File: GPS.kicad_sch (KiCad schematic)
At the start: 7 parts, among them Q3 BC817

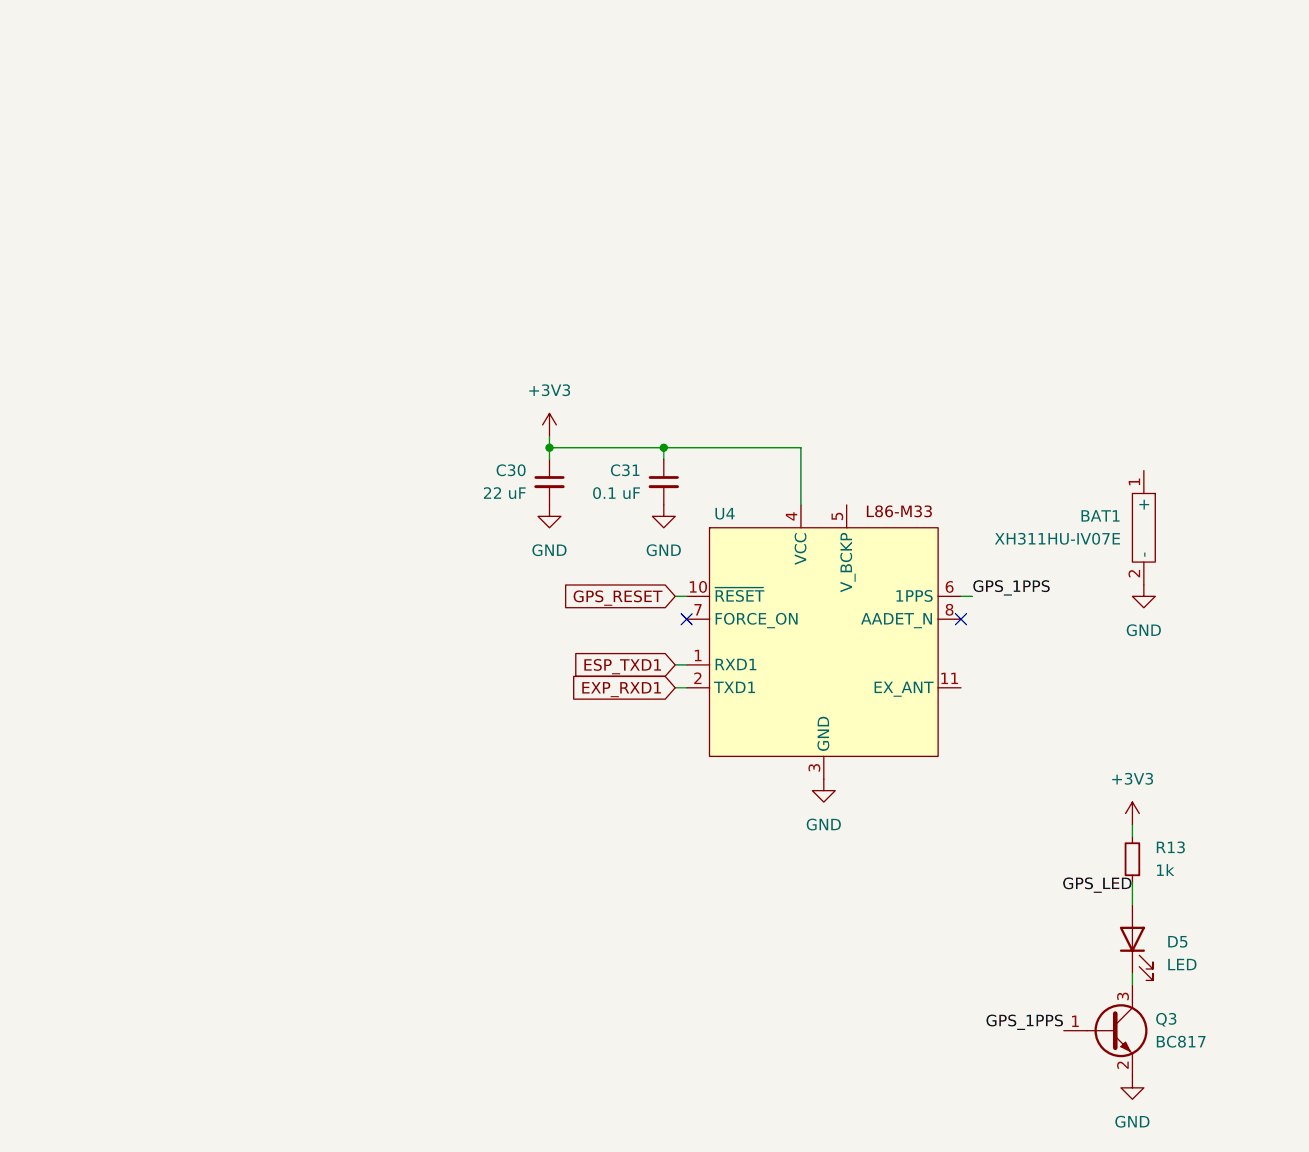
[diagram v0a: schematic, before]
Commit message: Wired barometers and GPS up, added misc LEDs, tidy-up
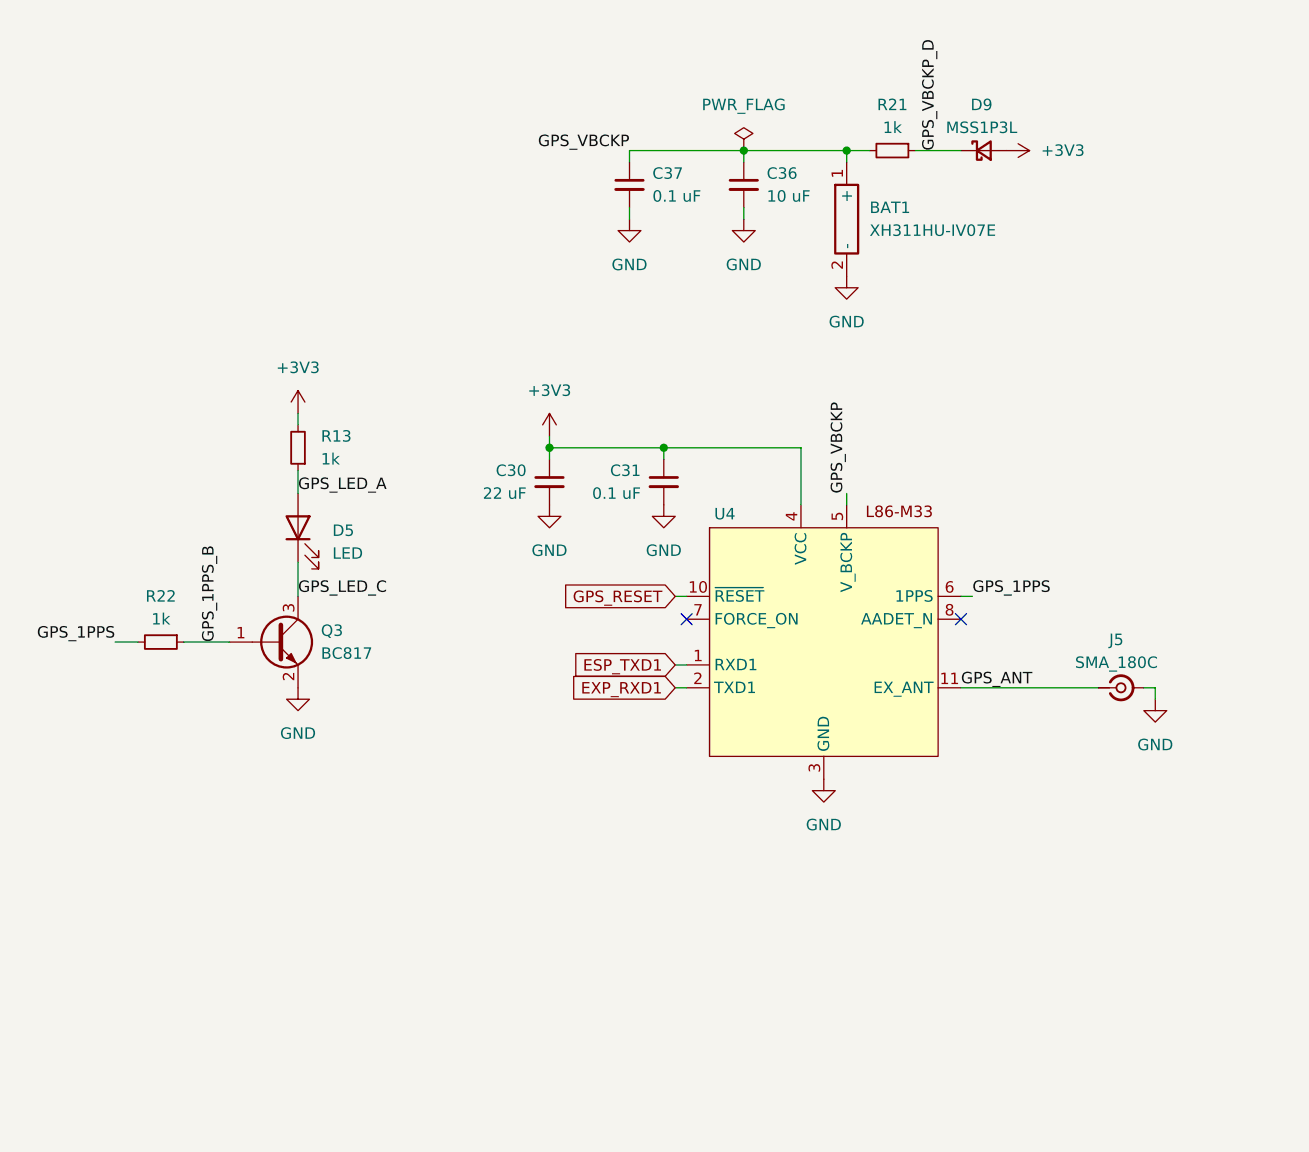
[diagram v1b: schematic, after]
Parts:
- added C36: 10 uF, symbol Device:C_Small
- added C37: 0.1 uF, Capacitor_SMD:C_0805_2012Metric, symbol Device:C_Small
- added D9: MSS1P3L, Diode_SMD:D_MicroSMP_AK, symbol Device:D_Schottky_Small
- added J5: SMA_180C, Valkyrie_footprints:SMA_180C, symbol Connector:Conn_Coaxial_Small
- added R21, R22: 1k, symbol Device:R_Small
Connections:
- net +3V3: now also D9.2 (A)
- net GND: now also C36.2, C37.2, J5.2 (Ext)
- net GPS_1PPS: now also R22.2; no longer Q3.1 (B)
- net GPS_LED_C: now reaches D5.1 (K), Q3.3 (C)
- net GPS_VBCKP: now reaches BAT1.1 (+)
- net GPS_VBCKP: now also U4.5 (V_BCKP), C36.1, C37.1, R21.2
- net GPS_ANT: now reaches U4.11 (EX_ANT)
- net GPS_ANT: now also J5.1 (In)
- net GPS_LED renamed GPS_LED_A
- new net GPS_1PPS_B: Q3.1 (B), R22.1
- new net GPS_VBCKP_D: D9.1 (K), R21.1
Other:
- moved on the sheet: BAT1, D5, Q3, R13

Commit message: preliminary schematic wired, all footprints assigned, all laid out in PCB editor.
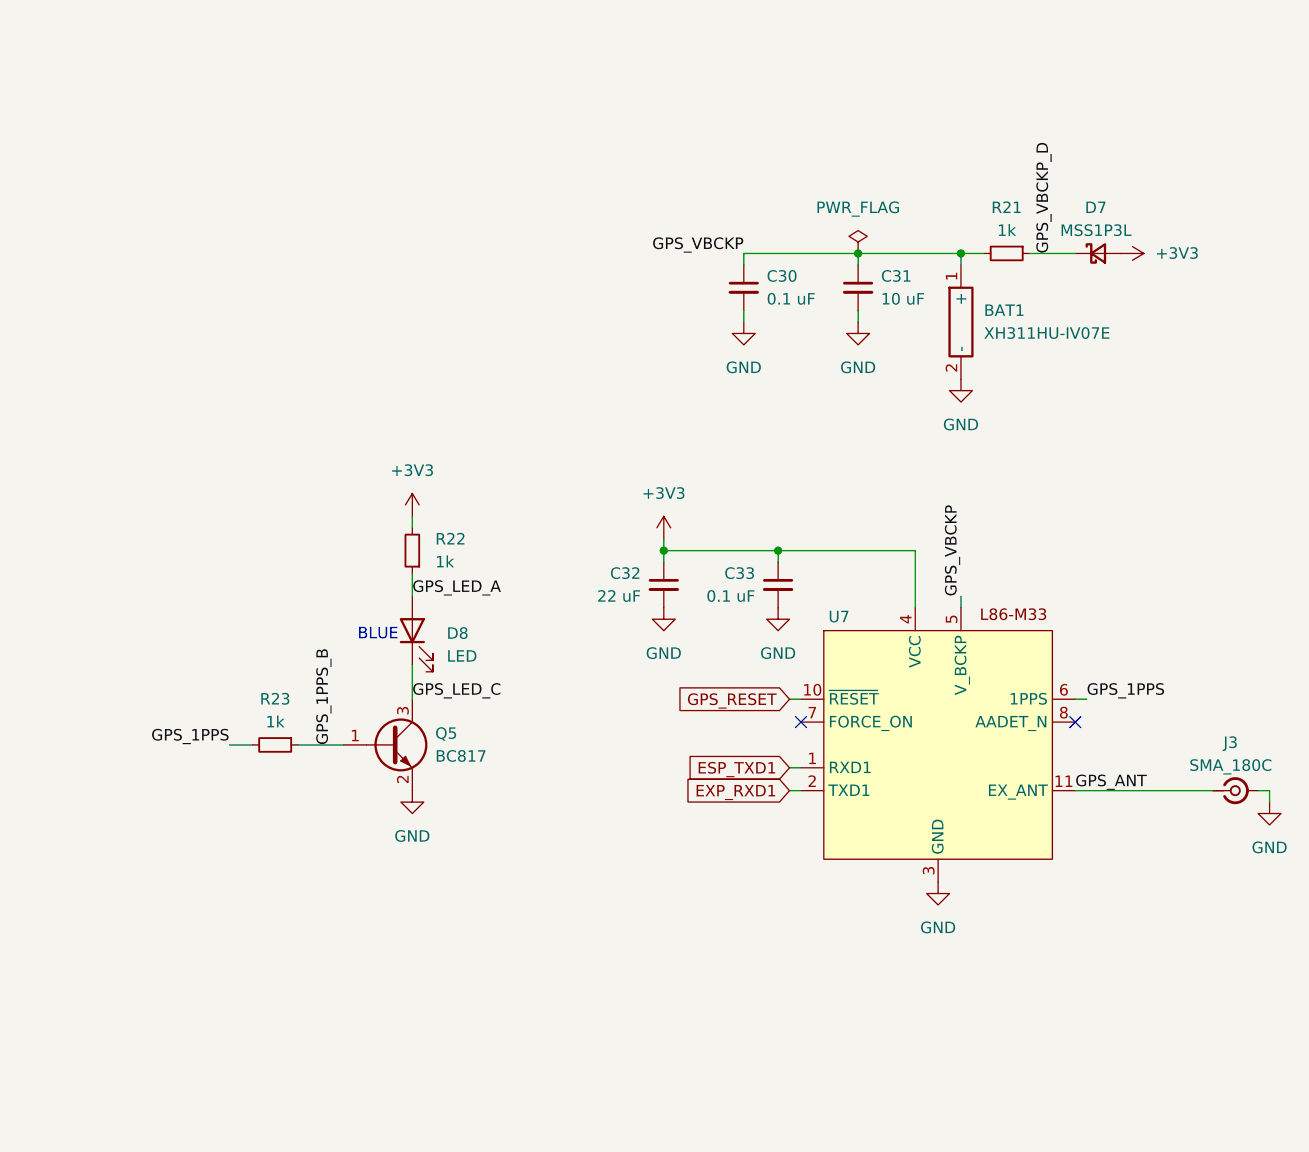
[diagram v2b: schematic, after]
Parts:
- C31: renamed from C36; footprint (none) -> Capacitor_SMD:C_0603_1608Metric
- C32: renamed from C30; footprint (none) -> Capacitor_SMD:C_0603_1608Metric
- R21: footprint (none) -> Resistor_SMD:R_0603_1608Metric
- R22: renamed from R13; footprint (none) -> Resistor_SMD:R_0603_1608Metric
- R23: renamed from R22; footprint (none) -> Resistor_SMD:R_0603_1608Metric
- renumbered C37 to C30, C31 to C33, D9 to D7, D5 to D8, J5 to J3, Q3 to Q5, U4 to U7
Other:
- note added: "BLUE"
- moved on the sheet: BAT1, C30, C31, C32, C33, D7, D8, J3, Q5, R21, R22, R23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

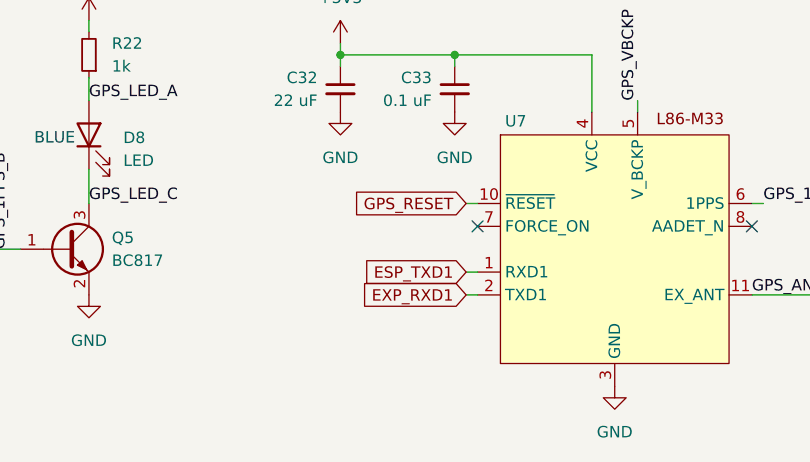
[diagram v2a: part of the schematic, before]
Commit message: reassigned some footprints, preliminary PCB layout
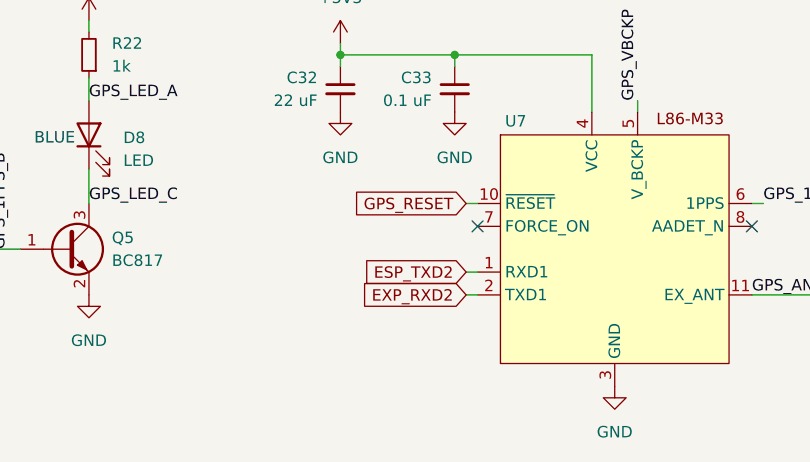
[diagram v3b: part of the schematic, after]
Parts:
- C30, C33: footprint Capacitor_SMD:C_0805_2012Metric -> Capacitor_SMD:C_0603_1608Metric
- D8: footprint LED_SMD:LED_0805_2012Metric -> LED_SMD:LED_0603_1608Metric
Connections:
- net ESP_TXD1 renamed ESP_TXD2
- net EXP_RXD1 renamed EXP_RXD2
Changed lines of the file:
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@@
 		)
 	)
-	(global_label "ESP_TXD1"
+	(global_label "ESP_TXD2"
 		(shape input)
 		(at 133.35 101.6 180)
@@
 		)
 	)
-	(global_label "EXP_RXD1"
+	(global_label "EXP_RXD2"
 		(shape input)
 		(at 133.35 104.14 180)
@@
 			)
 		)
-		(property "Footprint" "Capacitor_SMD:C_0805_2012Metric"
+		(property "Footprint" "Capacitor_SMD:C_0603_1608Metric"
 			(at 128.27 48.26 0)
 			(effects
@@
 			)
 		)
-		(property "Footprint" "Capacitor_SMD:C_0805_2012Metric"
+		(property "Footprint" "Capacitor_SMD:C_0603_1608Metric"
 			(at 132.08 81.28 0)
 			(effects
@@
 			)
 		)
-		(property "Footprint" "LED_SMD:LED_0805_2012Metric"
+		(property "Footprint" "LED_SMD:LED_0603_1608Metric"
 			(at 91.44 86.36 0)
 			(effects

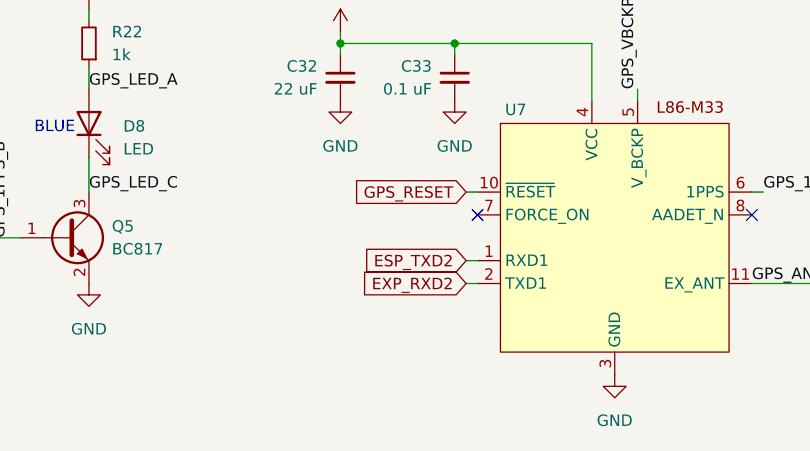
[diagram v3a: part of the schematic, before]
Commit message: added missing output diodes, added 3d models, misc. re-laying
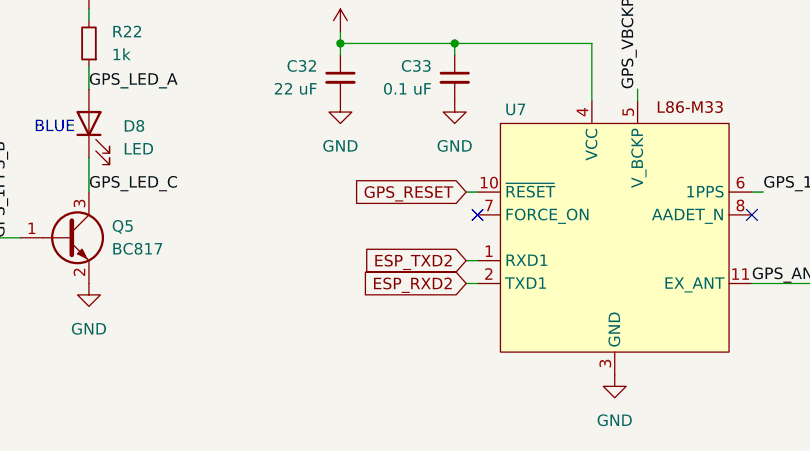
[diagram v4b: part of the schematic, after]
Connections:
- net EXP_RXD2 renamed ESP_RXD2
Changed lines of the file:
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@@
 		)
 	)
-	(global_label "EXP_RXD2"
+	(global_label "ESP_RXD2"
 		(shape input)
 		(at 133.35 104.14 180)

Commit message: did some clean-up, did some to-do tasks.
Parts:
- J3: footprint Valkyrie_footprints:SMA_180C -> Connector_Coaxial:SMA_Amphenol_132134-16_Vertical
- renumbered D7 to D8, D8 to D9
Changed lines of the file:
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@@
 		(dnp no)
 		(fields_autoplaced yes)
-		(property "Reference" "#PWR077"
+		(property "Reference" "#PWR080"
 			(at 119.38 80.01 0)
 			(effects
@@
 			(project "valkyriev3"
 				(path "/d24fd15c-a242-4d26-9876-7755ca0d378c/00fc6d2a-79f7-4b02-8c94-ea393adce81b"
-					(reference "#PWR077")
+					(reference "#PWR080")
 					(unit 1)
 				)
@@
 		(dnp no)
 		(fields_autoplaced yes)
-		(property "Reference" "#PWR073"
+		(property "Reference" "#PWR076"
 			(at 128.27 58.42 0)
 			(effects
@@
 			(project "valkyriev3"
 				(path "/d24fd15c-a242-4d26-9876-7755ca0d378c/00fc6d2a-79f7-4b02-8c94-ea393adce81b"
-					(reference "#PWR073")
+					(reference "#PWR076")
 					(unit 1)
 				)
@@
 		(dnp no)
 		(fields_autoplaced yes)
-		(property "Reference" "#PWR081"
+		(property "Reference" "#PWR084"
 			(at 186.69 111.76 0)
 			(effects
@@
 			(project "valkyriev3"
 				(path "/d24fd15c-a242-4d26-9876-7755ca0d378c/00fc6d2a-79f7-4b02-8c94-ea393adce81b"
-					(reference "#PWR081")
+					(reference "#PWR084")
 					(unit 1)
 				)
@@
 			)
 		)
-		(property "Footprint" "Valkyrie_footprints:SMA_180C"
+		(property "Footprint" "Connector_Coaxial:SMA_Amphenol_132134-16_Vertical"
 			(at 182.88 104.14 0)
 			(effects
@@
 		(dnp no)
 		(fields_autoplaced yes)
-		(property "Reference" "D8"
+		(property "Reference" "D9"
 			(at 95.25 86.6774 90)
 			(effects
@@
 			(project "valkyriev3"
 				(path "/d24fd15c-a242-4d26-9876-7755ca0d378c/00fc6d2a-79f7-4b02-8c94-ea393adce81b"
-					(reference "D8")
+					(reference "D9")
 					(unit 1)
 				)
@@
 		(dnp no)
 		(fields_autoplaced yes)
-		(property "Reference" "#PWR072"
+		(property "Reference" "#PWR075"
 			(at 166.37 44.45 0)
 			(effects
@@
 			(project "valkyriev3"
 				(path "/d24fd15c-a242-4d26-9876-7755ca0d378c/00fc6d2a-79f7-4b02-8c94-ea393adce81b"
-					(reference "#PWR072")
+					(reference "#PWR075")
 					(unit 1)
 				)
@@
 		(dnp no)
 		(fields_autoplaced yes)
-		(property "Reference" "#PWR079"
+		(property "Reference" "#PWR082"
 			(at 132.08 90.17 0)
 			(effects
@@
 			(project "valkyriev3"
 				(path "/d24fd15c-a242-4d26-9876-7755ca0d378c/00fc6d2a-79f7-4b02-8c94-ea393adce81b"
-					(reference "#PWR079")
+					(reference "#PWR082")
 					(unit 1)
 				)
@@
 		(dnp no)
 		(fields_autoplaced yes)
-		(property "Reference" "#PWR074"
+		(property "Reference" "#PWR077"
 			(at 140.97 58.42 0)
 			(effects
@@
 			(project "valkyriev3"
 				(path "/d24fd15c-a242-4d26-9876-7755ca0d378c/00fc6d2a-79f7-4b02-8c94-ea393adce81b"
-					(reference "#PWR074")
+					(reference "#PWR077")
 					(unit 1)
 				)
@@
 		(dnp no)
 		(fields_autoplaced yes)
-		(property "Reference" "#PWR082"
+		(property "Reference" "#PWR085"
 			(at 149.86 120.65 0)
 			(effects
@@
 			(project ""
 				(path "/d24fd15c-a242-4d26-9876-7755ca0d378c/00fc6d2a-79f7-4b02-8c94-ea393adce81b"
-					(reference "#PWR082")
+					(reference "#PWR085")
 					(unit 1)
 				)
@@
 		(dnp no)
 		(fields_autoplaced yes)
-		(property "Reference" "#PWR076"
+		(property "Reference" "#PWR079"
 			(at 91.44 77.47 0)
 			(effects
@@
 			(project "valkyriev3"
 				(path "/d24fd15c-a242-4d26-9876-7755ca0d378c/00fc6d2a-79f7-4b02-8c94-ea393adce81b"
-					(reference "#PWR076")
+					(reference "#PWR079")
 					(unit 1)
 				)
@@
 		(dnp no)
 		(fields_autoplaced yes)
-		(property "Reference" "#PWR078"
+		(property "Reference" "#PWR081"
 			(at 119.38 90.17 0)
 			(effects
@@
 			(project "valkyriev3"
 				(path "/d24fd15c-a242-4d26-9876-7755ca0d378c/00fc6d2a-79f7-4b02-8c94-ea393adce81b"
-					(reference "#PWR078")
+					(reference "#PWR081")
 					(unit 1)
 				)
@@
 		(on_board yes)
 		(dnp no)
-		(property "Reference" "D7"
+		(property "Reference" "D8"
 			(at 167.386 39.37 0)
 			(effects
@@
 			(project ""
 				(path "/d24fd15c-a242-4d26-9876-7755ca0d378c/00fc6d2a-79f7-4b02-8c94-ea393adce81b"
-					(reference "D7")
+					(reference "D8")
 					(unit 1)
 				)
@@
 		(dnp no)
 		(fields_autoplaced yes)
-		(property "Reference" "#PWR075"
+		(property "Reference" "#PWR078"
 			(at 152.4 64.77 0)
 			(effects
@@
 			(project "valkyriev3"
 				(path "/d24fd15c-a242-4d26-9876-7755ca0d378c/00fc6d2a-79f7-4b02-8c94-ea393adce81b"
-					(reference "#PWR075")
+					(reference "#PWR078")
 					(unit 1)
 				)
@@
 		(dnp no)
 		(fields_autoplaced yes)
-		(property "Reference" "#PWR080"
+		(property "Reference" "#PWR083"
 			(at 91.44 110.49 0)
 			(effects
@@
 			(project "valkyriev3"
 				(path "/d24fd15c-a242-4d26-9876-7755ca0d378c/00fc6d2a-79f7-4b02-8c94-ea393adce81b"
-					(reference "#PWR080")
-					(unit 1)
-				)
+					(reference "#PWR083")
+					(unit 1)
+				)
